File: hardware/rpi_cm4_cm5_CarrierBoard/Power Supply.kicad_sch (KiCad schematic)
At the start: 104 parts, among them J15 TB002-500-02BE, Q1 DMPH6050SK3-13, Q2 2N7002, Q3 2N7002, Q7 2N7002, U10 TPS54527DDAR, U11 TPS54527DDAR, U12 TPS7A7001DDAR, U13 INA180A2IDBVR, U14 INA180A2IDBVR, U2 SN74LVC1G14DBVR, U28 INA180A2IDBVR, U29 INA180A2IDBVR, U3 SE555DR, U9 TPS54527DDAR

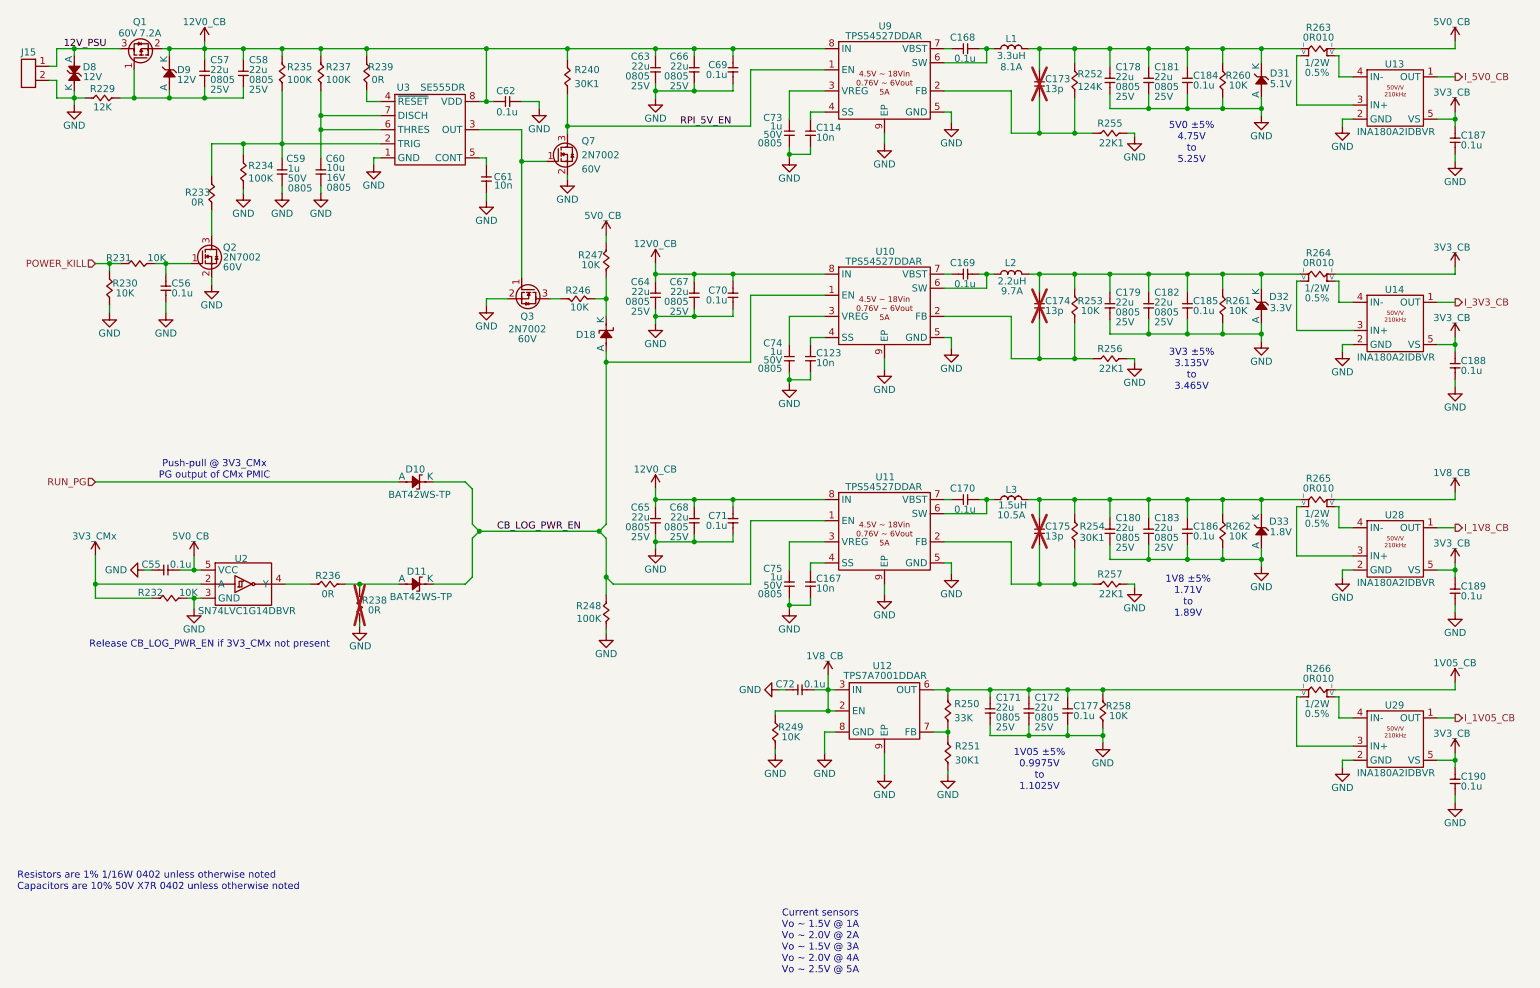
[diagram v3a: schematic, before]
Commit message: Modify power supply page (input capacitors to buck regulator), update PCB stackup (6-layer JLC 061611-7628 1oz int, 1oz ext, 1.6mm ±10%)
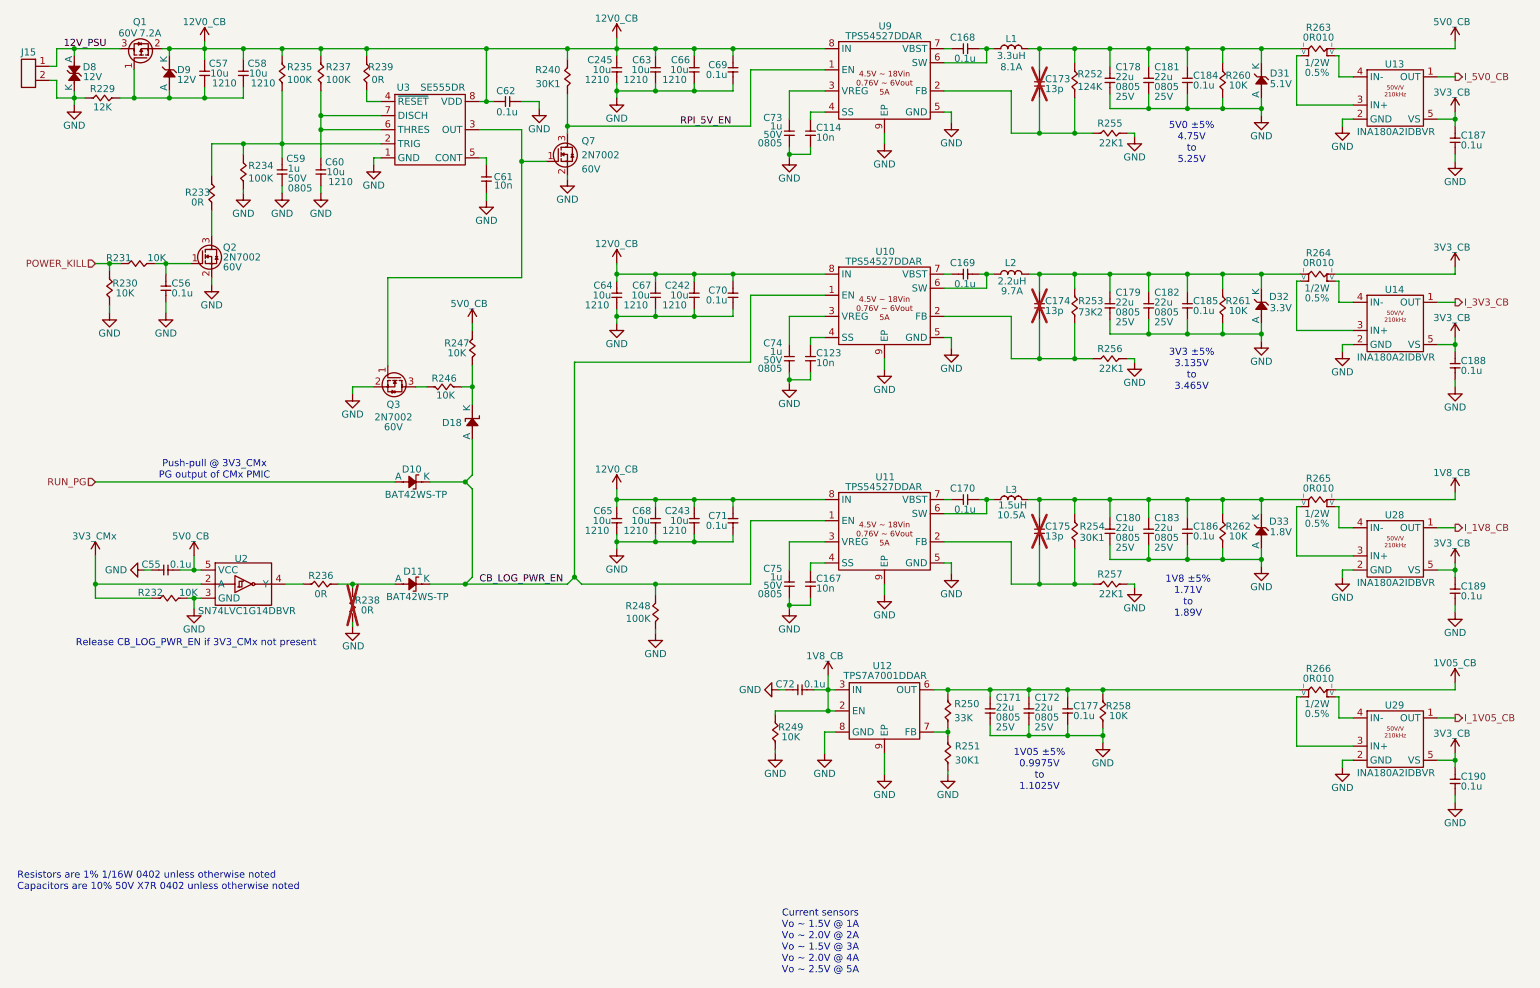
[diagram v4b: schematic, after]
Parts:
- removed C57, C58, C63, C64, C65, C66, C67, C68: 22u, footprint:CAP_NONPOL_0805, symbol KicadCompDb:Capacitors/CAP_CER_SMT_00011
- removed C60: 10u, footprint:CAP_NONPOL_0805, symbol KicadCompDb:Capacitors/CAP_CER_SMT_00004
- removed R253: 10K, footprint:RES_0402, symbol KicadCompDb:Resistors/RES_SMT_00013
- added C242, C243, C245, C57, C58, C60, C63, C64, C65, C66, C67, C68: 10u, footprint:CAP_NONPOL_1210, symbol KicadCompDb:Capacitors/CAP_CER_SMT_00014
- added R253: 73K2, footprint:RES_0402, symbol KicadCompDb:Resistors/RES_SMT_00032
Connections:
- net 12V0_CB: now also C242.2, C243.2, C245.2, C57.2, C58.2, C63.2, C64.2, C65.2, C66.2, C67.2, C68.2
- net GND: now also C242.1, C243.1, C245.1, C60.1, C63.1, C64.1, C65.1, C66.1, C67.1, C68.1
- net at C174.1, R256.1, U10.2 (FB): now also R253.1
- net at D9.2 (A), Q1.1 (G), R229.2: now also C57.1, C58.1
- net at C174.2, C179.2, C182.2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: now also R253.2
- net at R237.1, U3.6 (THRES), U3.7 (DISCH): now also C60.2
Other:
- moved on the sheet: D10, D11, D18, Q3, R236, R238, R240, R246, R247, R248

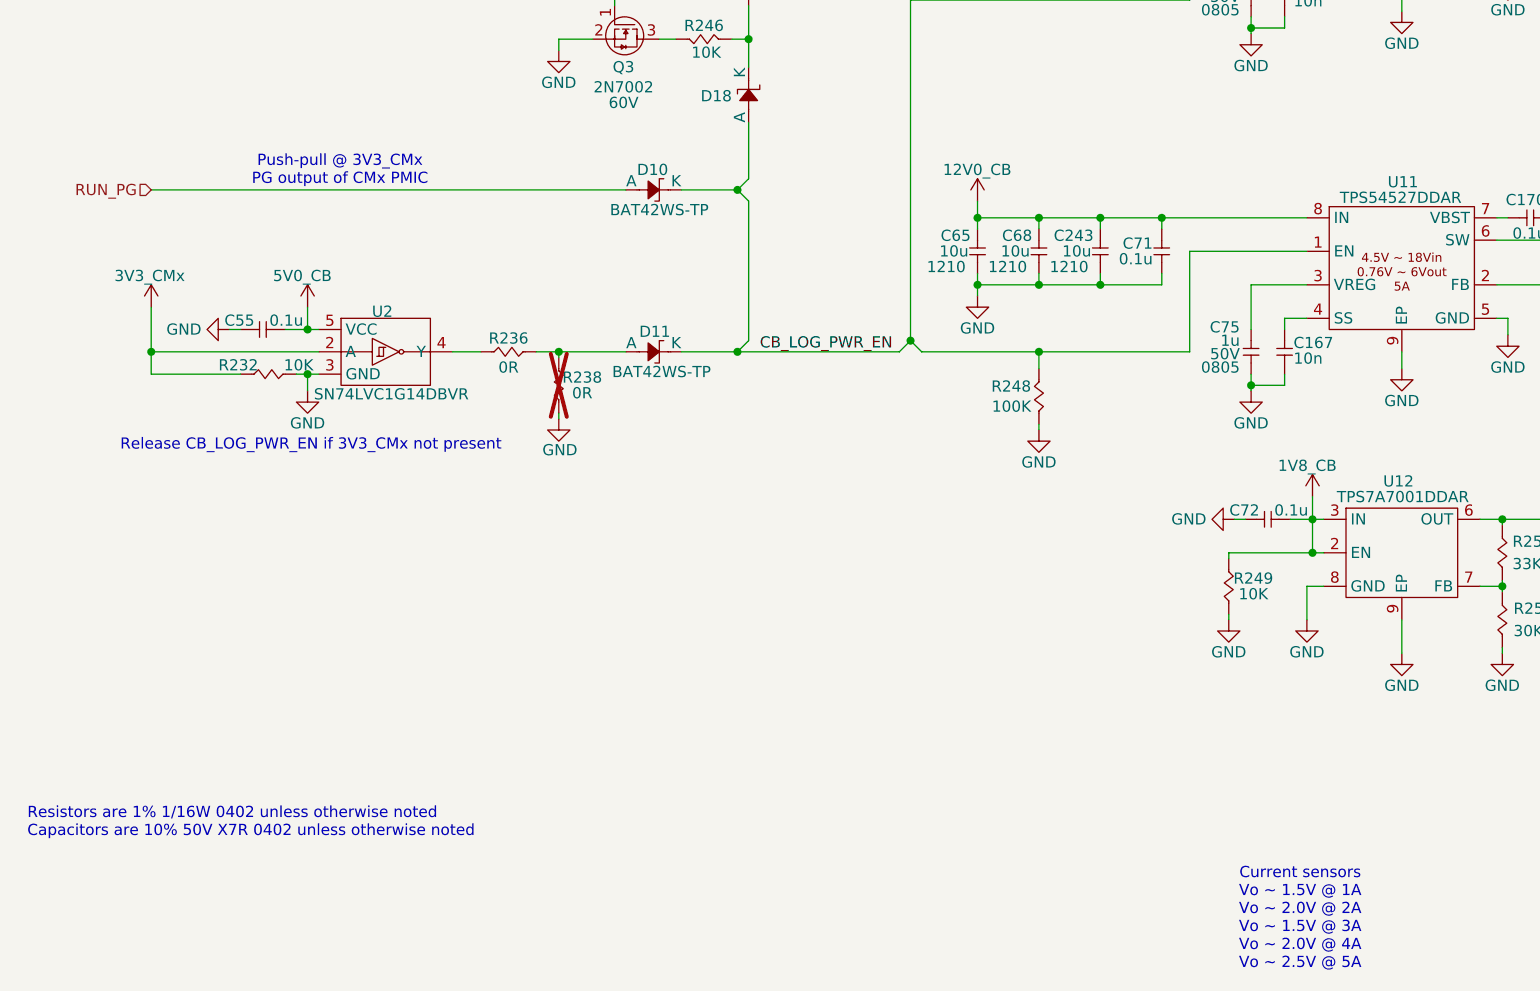
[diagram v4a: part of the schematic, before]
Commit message: Add preliminary BOM and preliminary .pdf schmematics Add BOM option for I2C control of ILI2132A for CapTouch HMI Add BOM options and DNP / 0R resistors for CM4 - CM5 build options
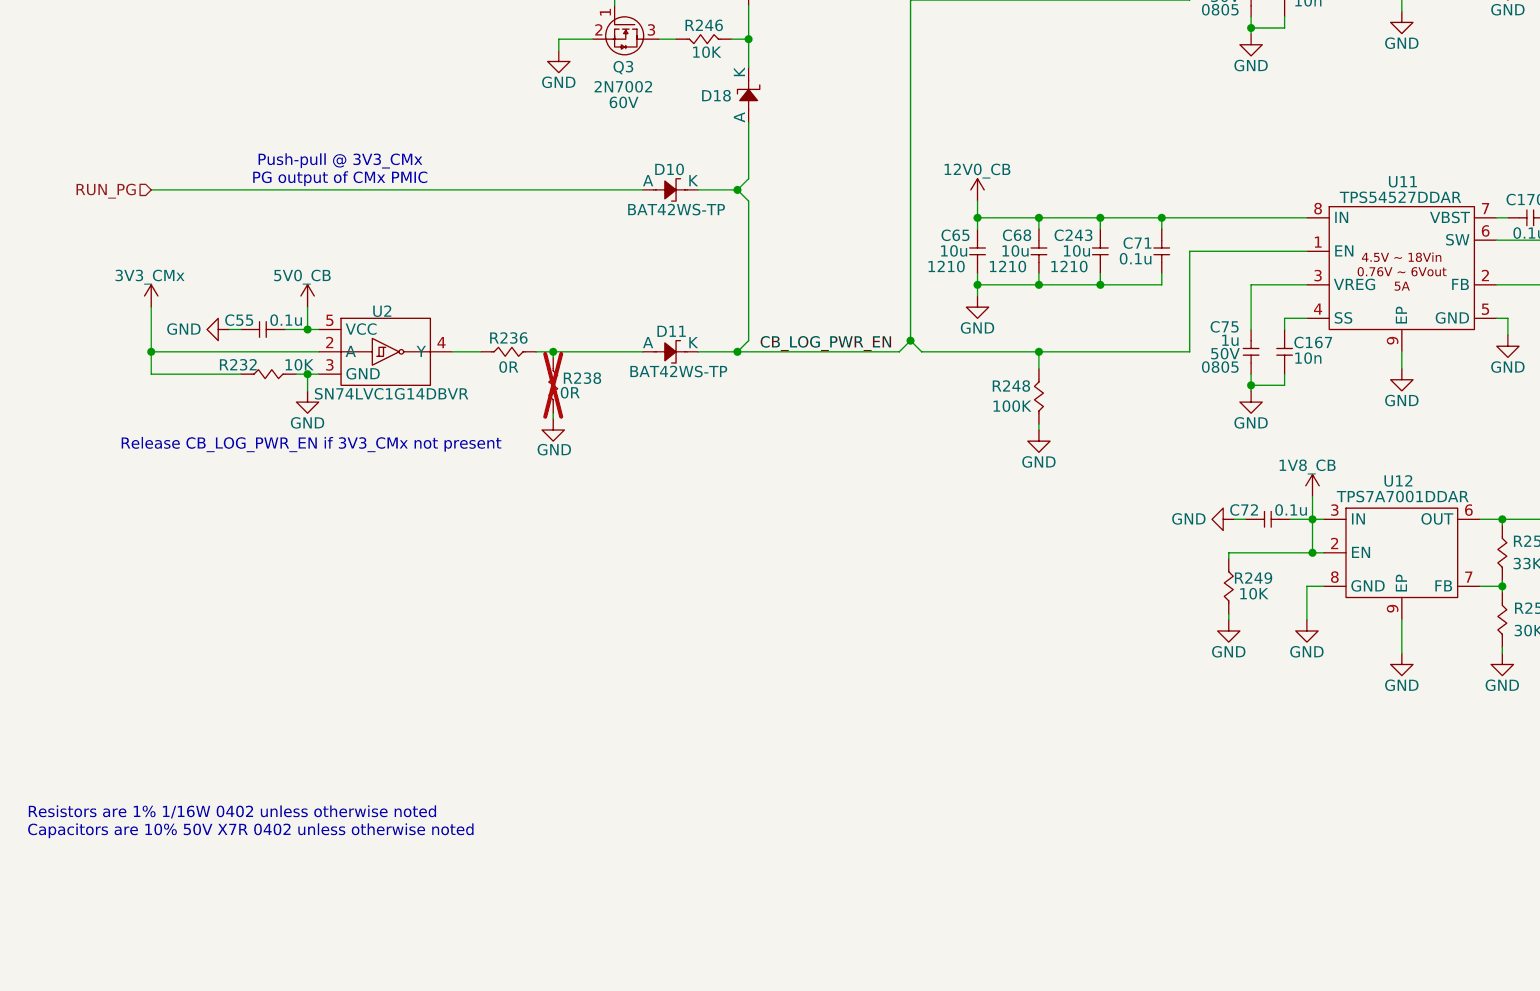
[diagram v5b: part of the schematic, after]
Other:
- note removed: "Current sensors Vo ~ 1.5V @ 1A Vo ~ 2.0V @ 2A Vo ~ 1.5V @ 3A Vo ~ 2.0V @ 4A Vo ~ 2.5V @ 5A"
- moved on the sheet: D10, D11, R238

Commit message: Added power input protection & filter Added dedicated QWIIC connector on RPI CMx I2C6 bus Adjusted power table and PinMux Updated schematics accordingly
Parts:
- removed D8: SMAJ12CA, footprint:DO-214AC, symbol KicadCompDb:ESD Diodes/ESD_DIODE_00005
- removed D9: MMSZ5242B-TP, footprint:SOD-123, symbol KicadCompDb:Diodes/DIODE_00003
- removed J15: TB002-500-02BE, footprint:TB002-500-02BE, symbol KicadCompDb:Connector/CONN_00018
- removed Q1: DMPH6050SK3-13, footprint:TO-252-3, symbol KicadCompDb:Mosfet/MOSFET_00003
- removed R229: 12K, footprint:RES_0402, symbol KicadCompDb:Resistors/RES_SMT_00014
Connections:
- net GND: now also C57.1, C58.1
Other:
- note removed: "5V0 ±5% 4.75V to 5.25V"
